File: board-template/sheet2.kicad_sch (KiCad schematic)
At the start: 0 parts

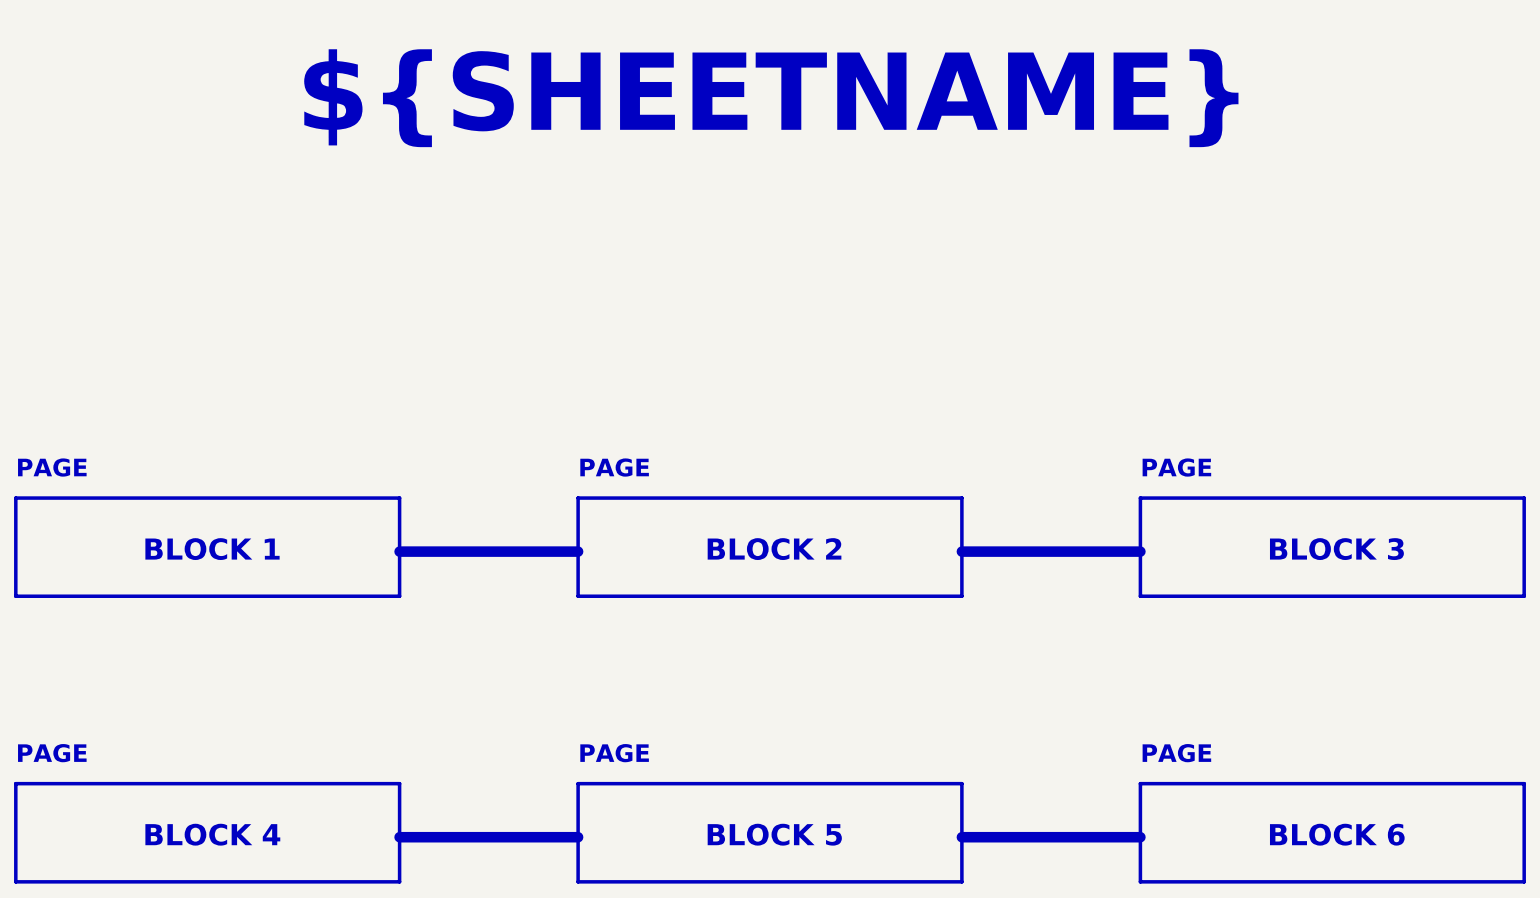
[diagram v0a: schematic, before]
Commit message: template(refact): improve block diagram and power budget
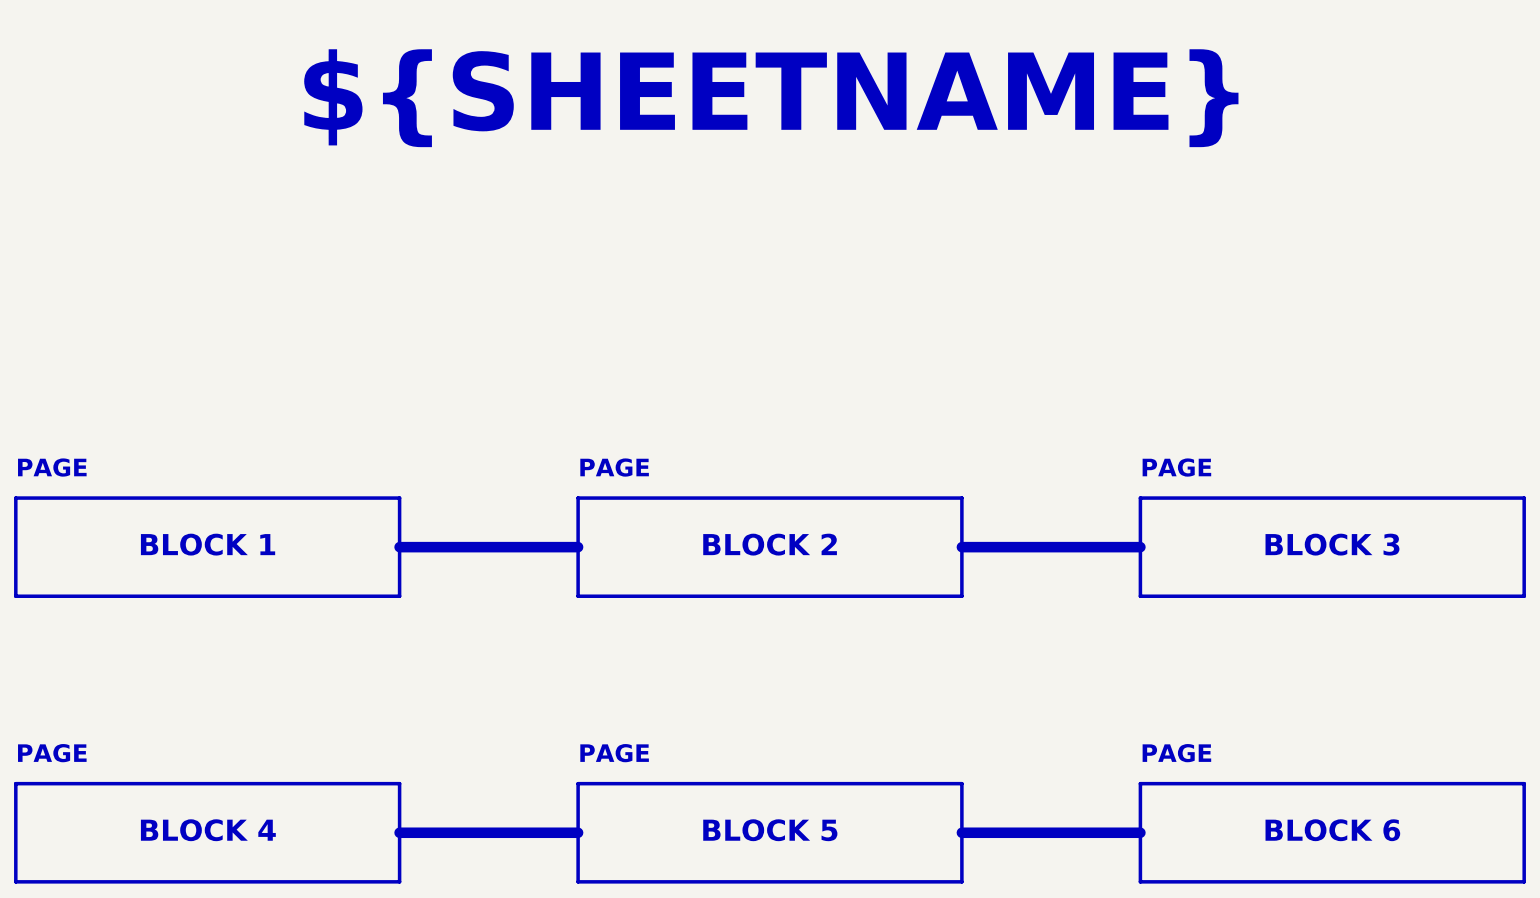
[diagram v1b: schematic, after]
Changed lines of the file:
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@@
 				(size 11 11)
 				(bold yes)
-				(color 0 0 0 1)
+				(color 162 22 34 1)
 			)
 			(justify bottom)
@@
 	(rectangle
 		(start 40.64 83.82)
-		(end 95.25 97.78999999999999)
-		(stroke
-			(width 0.5)
-			(type solid)
-			(color 0 0 0 1)
-		)
-		(fill
-			(type none)
+		(end 95.25 97.79)
+		(stroke
+			(width 0.5)
+			(type solid)
+			(color 0 0 0 1)
+		)
+		(fill
+			(type color)
+			(color 255 255 194 1)
 		)
 	)
 	(text "BLOCK 1"
 		(exclude_from_sim no)
-		(at 68.58 91.44 0)
-		(effects
-			(font
-				(face "Arial")
-				(size 3 3)
-				(bold yes)
-				(color 0 0 0 1)
-			)
-		)
-	)
-	(text "PAGE"
-		(exclude_from_sim no)
-		(at 40.64 81.27999999999999 0)
+		(at 67.945 90.805 0)
+		(effects
+			(font
+				(face "Arial")
+				(size 3 3)
+				(bold yes)
+				(color 0 0 0 1)
+			)
+		)
+	)
+	(text "PAGE"
+		(exclude_from_sim no)
+		(at 40.64 81.28 0)
 		(effects
 			(font
@@
 	(rectangle
 		(start 120.65 83.82)
-		(end 175.26 97.78999999999999)
-		(stroke
-			(width 0.5)
-			(type solid)
-			(color 0 0 0 1)
-		)
-		(fill
-			(type none)
+		(end 175.26 97.79)
+		(stroke
+			(width 0.5)
+			(type solid)
+			(color 0 0 0 1)
+		)
+		(fill
+			(type color)
+			(color 72 72 72 1)
 		)
 	)
 	(text "BLOCK 2"
 		(exclude_from_sim no)
-		(at 148.59 91.44 0)
-		(effects
-			(font
-				(face "Arial")
-				(size 3 3)
-				(bold yes)
-				(color 0 0 0 1)
-			)
-		)
-	)
-	(text "PAGE"
-		(exclude_from_sim no)
-		(at 120.65 81.27999999999999 0)
-		(effects
-			(font
-				(face "Arial")
-				(size 2.5 2.5)
-				(bold yes)
-				(color 0 0 0 1)
-			)
-			(justify left bottom)
-		)
-	)
-	(polyline
-		(pts
-			(xy 95.25 91.44)
-			(xy 120.65 91.44)
+		(at 147.955 90.805 0)
+		(effects
+			(font
+				(face "Arial")
+				(size 3 3)
+				(bold yes)
+				(color 255 255 255 1)
+			)
+		)
+	)
+	(text "PAGE"
+		(exclude_from_sim no)
+		(at 120.65 81.28 0)
+		(effects
+			(font
+				(face "Arial")
+				(size 2.5 2.5)
+				(bold yes)
+				(color 0 0 0 1)
+			)
+			(justify left bottom)
+		)
+	)
+	(polyline
+		(pts
+			(xy 95.25 90.805)
+			(xy 120.65 90.805)
 		)
 		(stroke
@@
 	(rectangle
 		(start 200.66 83.82)
-		(end 255.26999999999998 97.78999999999999)
-		(stroke
-			(width 0.5)
-			(type solid)
-			(color 0 0 0 1)
-		)
-		(fill
-			(type none)
+		(end 255.27 97.79)
+		(stroke
+			(width 0.5)
+			(type solid)
+			(color 0 0 0 1)
+		)
+		(fill
+			(type color)
+			(color 194 194 194 1)
 		)
 	)
 	(text "BLOCK 3"
 		(exclude_from_sim no)
-		(at 228.6 91.44 0)
-		(effects
-			(font
-				(face "Arial")
-				(size 3 3)
-				(bold yes)
-				(color 0 0 0 1)
-			)
-		)
-	)
-	(text "PAGE"
-		(exclude_from_sim no)
-		(at 200.66 81.27999999999999 0)
-		(effects
-			(font
-				(face "Arial")
-				(size 2.5 2.5)
-				(bold yes)
-				(color 0 0 0 1)
-			)
-			(justify left bottom)
-		)
-	)
-	(polyline
-		(pts
-			(xy 175.26 91.44)
-			(xy 200.66 91.44)
+		(at 227.965 90.805 0)
+		(effects
+			(font
+				(face "Arial")
+				(size 3 3)
+				(bold yes)
+				(color 0 0 0 1)
+			)
+		)
+	)
+	(text "PAGE"
+		(exclude_from_sim no)
+		(at 200.66 81.28 0)
+		(effects
+			(font
+				(face "Arial")
+				(size 2.5 2.5)
+				(bold yes)
+				(color 0 0 0 1)
+			)
+			(justify left bottom)
+		)
+	)
+	(polyline
+		(pts
+			(xy 175.26 90.805)
+			(xy 200.66 90.805)
 		)
 		(stroke
@@
 		)
 		(fill
-			(type none)
+			(type color)
+			(color 255 255 194 1)
 		)
 	)
 	(text "BLOCK 4"
 		(exclude_from_sim no)
-		(at 68.58 132.07999999999998 0)
-		(effects
-			(font
-				(face "Arial")
-				(size 3 3)
-				(bold yes)
-				(color 0 0 0 1)
-			)
-		)
-	)
-	(text "PAGE"
-		(exclude_from_sim no)
-		(at 40.64 121.91999999999999 0)
+		(at 67.945 131.445 0)
+		(effects
+			(font
+				(face "Arial")
+				(size 3 3)
+				(bold yes)
+				(color 0 0 0 1)
+			)
+		)
+	)
+	(text "PAGE"
+		(exclude_from_sim no)
+		(at 40.64 121.92 0)
 		(effects
 			(font
@@
 		)
 		(fill
-			(type none)
+			(type color)
+			(color 72 72 72 1)
 		)
 	)
 	(text "BLOCK 5"
 		(exclude_from_sim no)
-		(at 148.59 132.07999999999998 0)
-		(effects
-			(font
-				(face "Arial")
-				(size 3 3)
-				(bold yes)
-				(color 0 0 0 1)
-			)
-		)
-	)
-	(text "PAGE"
-		(exclude_from_sim no)
-		(at 120.65 121.91999999999999 0)
-		(effects
-			(font
-				(face "Arial")
-				(size 2.5 2.5)
-				(bold yes)
-				(color 0 0 0 1)
-			)
-			(justify left bottom)
-		)
-	)
-	(polyline
-		(pts
-			(xy 95.25 132.07999999999998)
-			(xy 120.65 132.07999999999998)
+		(at 147.955 131.445 0)
+		(effects
+			(font
+				(face "Arial")
+				(size 3 3)
+				(bold yes)
+				(color 255 255 255 1)
+			)
+		)
+	)
+	(text "PAGE"
+		(exclude_from_sim no)
+		(at 120.65 121.92 0)
+		(effects
+			(font
+				(face "Arial")
+				(size 2.5 2.5)
+				(bold yes)
+				(color 0 0 0 1)
+			)
+			(justify left bottom)
+		)
+	)
+	(polyline
+		(pts
+			(xy 95.25 131.445)
+			(xy 120.65 131.445)
 		)
 		(stroke
@@
 	(rectangle
 		(start 200.66 124.46)
-		(end 255.26999999999998 138.43)
-		(stroke
-			(width 0.5)
-			(type solid)
-			(color 0 0 0 1)
-		)
-		(fill
-			(type none)
+		(end 255.27 138.43)
+		(stroke
+			(width 0.5)
+			(type solid)
+			(color 0 0 0 1)
+		)
+		(fill
+			(type color)
+			(color 194 194 194 1)
 		)
 	)
 	(text "BLOCK 6"
 		(exclude_from_sim no)
-		(at 228.6 132.07999999999998 0)
-		(effects
-			(font
-				(face "Arial")
-				(size 3 3)
-				(bold yes)
-				(color 0 0 0 1)
-			)
-		)
-	)
-	(text "PAGE"
-		(exclude_from_sim no)
-		(at 200.66 121.91999999999999 0)
-		(effects
-			(font
-				(face "Arial")
-				(size 2.5 2.5)
-				(bold yes)
-				(color 0 0 0 1)
-			)
-			(justify left bottom)
-		)
-	)
-	(polyline
-		(pts
-			(xy 175.26 132.07999999999998)
-			(xy 200.66 132.07999999999998)
-		)
-		(stroke
+		(at 227.965 131.445 0)
+		(effects
+			(font
+				(face "Arial")
+				(size 3 3)
+				(bold yes)
+				(color 0 0 0 1)
+			)
+		)
+	)
+	(text "PAGE"
+		(exclude_from_sim no)
+		(at 200.66 121.92 0)
+		(effects
+			(font
+				(face "Arial")
+				(size 2.5 2.5)
+				(bold yes)
+				(color 0 0 0 1)
+			)
+			(justify left bottom)
+		)
+	)
+	(polyline
+		(pts
+			(xy 175.26 131.445)
+			(xy 200.66 131.445)
+		)
+		(stroke
